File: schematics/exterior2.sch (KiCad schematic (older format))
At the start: 56 parts

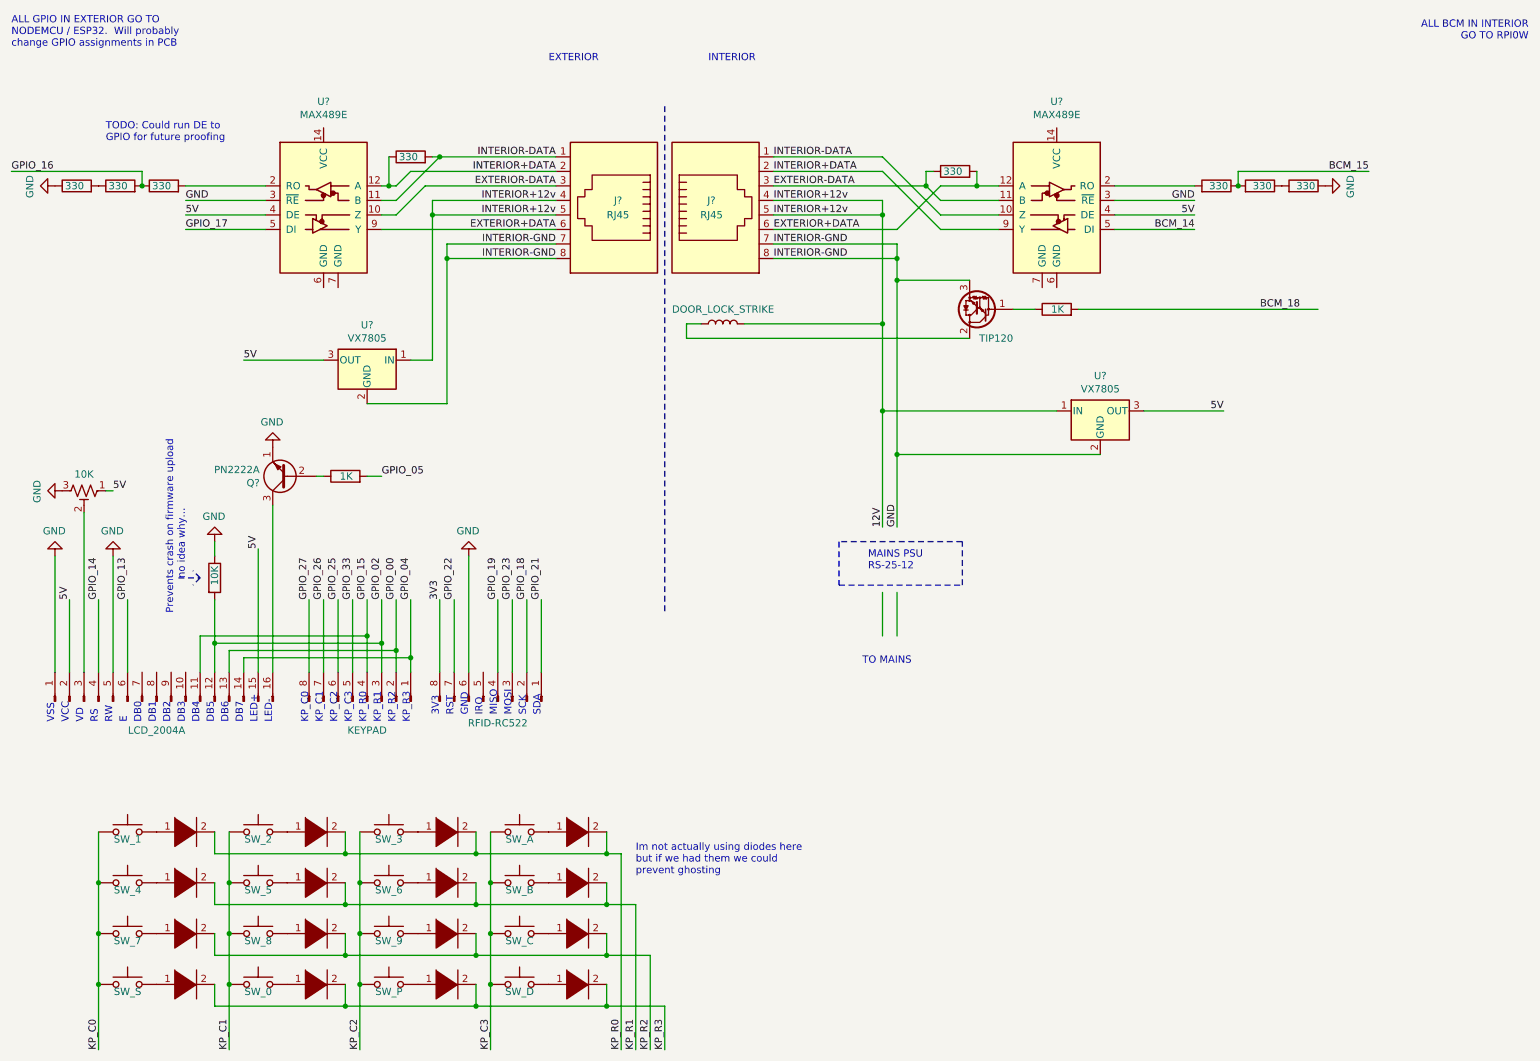
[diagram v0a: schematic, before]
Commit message: updated to verson 2 of hardware
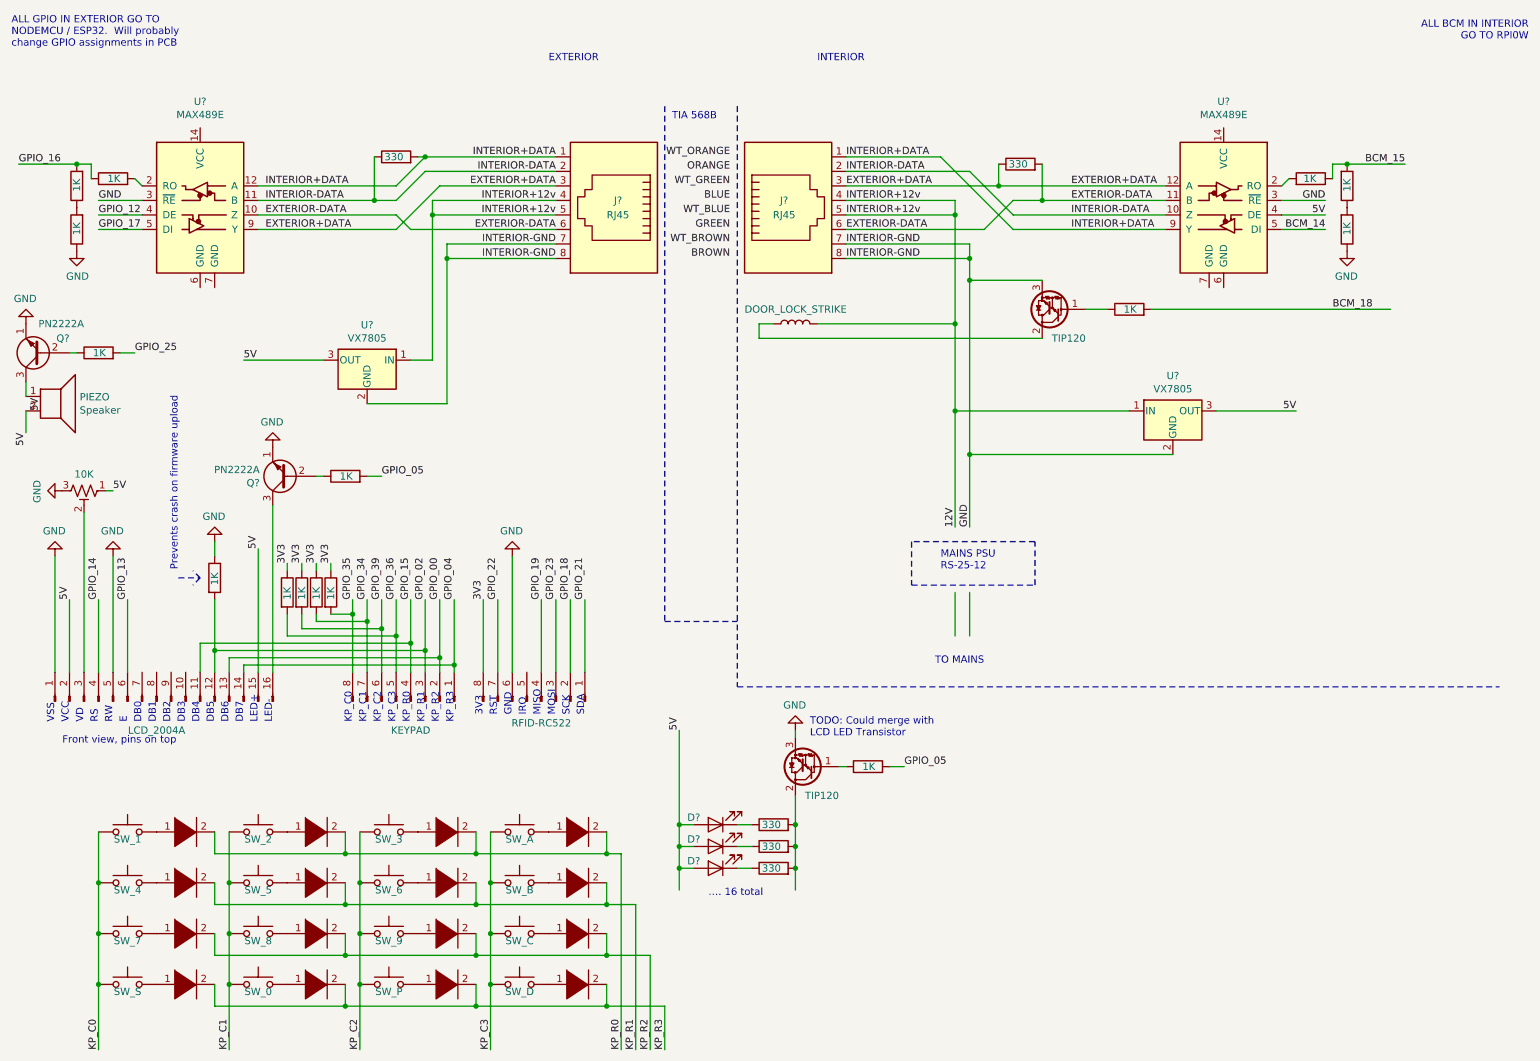
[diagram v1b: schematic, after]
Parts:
- removed R? (x3): 330, symbol Device:R
- added D? (x3): LED, symbol Device:LED
- added PIEZO: Speaker, symbol Device:Speaker
- added Q?: PN2222A, Package_TO_SOT_THT:TO-92_Inline, symbol Transistor_BJT:PN2222A
- added Q?: TIP120, Package_TO_SOT_THT:TO-220-3_Vertical, symbol Transistor_BJT:TIP120
- added R? (x9): 1K, symbol Device:R
- added R? (x3): 330, symbol Device:R
- R?: value 10K -> 1K
- R? (x3): value 330 -> 1K
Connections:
- net labels added: BLUE, BROWN, GPIO_12, GPIO_34, GPIO_35, GPIO_36, GPIO_39, GREEN, ORANGE, WT_BLUE, WT_BROWN, WT_GREEN, WT_ORANGE
- net labels removed: GPIO_26, GPIO_27, GPIO_33
- wire segments 168 -> 207
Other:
- note added: "Front view, pins on top"
- note added: "Prevents crash on firmware upload"
- note added: "TIA 568B"
- note added: "TODO: Could merge with \nLCD LED Transistor\n"
- note added: "…. 16 total"
- note removed: "Im not actually using diodes here\nbut if we had them we could\nprevent ghosting"
- note removed: "Prevents crash on firmware upload\n no idea why…\n"
- note removed: "TODO: Could run DE to\nGPIO for future proofing"
- moved on the sheet: DOOR_LOCK_STRIKE, J?, U?
